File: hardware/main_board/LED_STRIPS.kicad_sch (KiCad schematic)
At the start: 9 parts, among them IC801 SN74AHCT125DBR, J801 Conn_01x03_Pin, J802 Conn_01x03_Pin

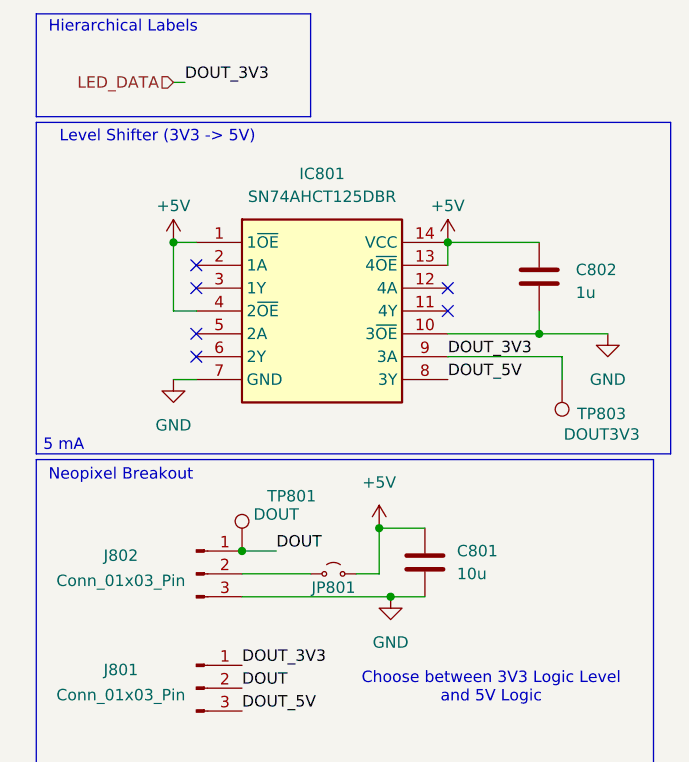
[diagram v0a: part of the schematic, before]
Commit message: changed level shifter. bunch of aesthetic changes. led resistors changed on main board. saving before nuke mouser.co.uk
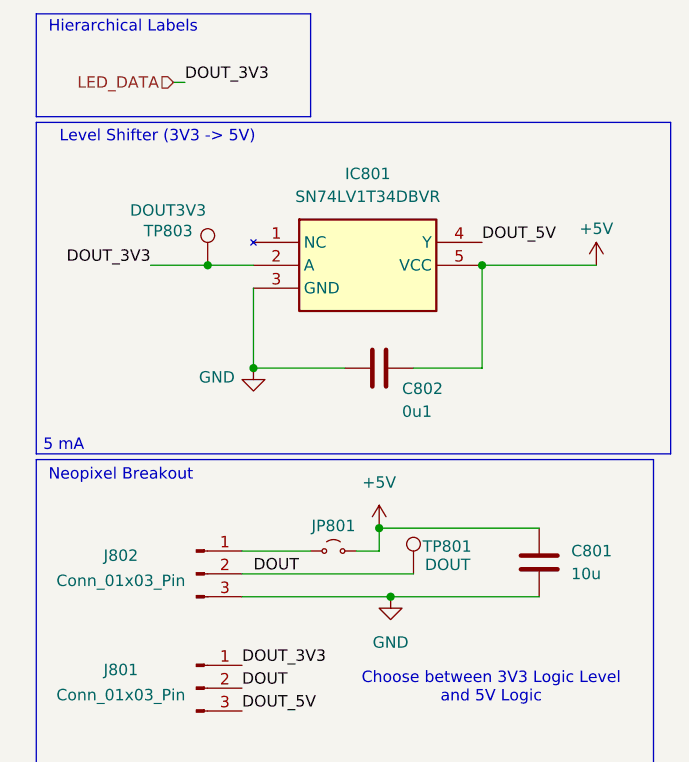
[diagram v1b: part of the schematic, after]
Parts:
- removed IC801: SN74AHCT125DBR, SamacSys_Parts:SOP65P780X200-14N, symbol SamacSys_Parts:SN74AHCT125DBR
- added IC801: SN74LV1T34DBVR, SamacSys_Parts:SOT95P280X145-5N, symbol SamacSys_Parts:SN74LV1T34DBVR
- C802: value 1u -> 0u1
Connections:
- net +5V: now also C802.2, IC801.5 (VCC); no longer C802.1
- net DOUT: now also J802.2 (Pin_2); no longer J802.1 (Pin_1)
- net DOUT_5V: now also IC801.4 (Y)
- net GND: now also C802.1, IC801.3 (GND); no longer C802.2
- net LED_DATA: now also IC801.2 (A)
- net at JP801.1 (A): now also J802.1 (Pin_1); no longer J802.2 (Pin_2)
- no-connect marks 6 -> 0
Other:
- moved on the sheet: C801, C802, JP801, TP801, TP803

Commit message: finished everything except bom information. drc verification
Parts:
- IC801: Mouser Price/Stock https://www.mouser.co.uk/ProductDetail/Texas-Instruments/SN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 -> https://www.mouser.com/ProductDetail/Texas-Instruments/SN74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
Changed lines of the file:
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@@
 			)
 		)
-		(property "Mouser Price/Stock" "https://www.mouser.co.uk/ProductDetail/Texas-Instruments/SN74LV1T34DBVR?qs=8sOby8ZxZLE4ekkxA3S6Wg%3D%3D"
+		(property "Mouser Price/Stock" "https://www.mouser.com/ProductDetail/Texas-Instruments/SN74LV1T34DBVR?qs=8sOby8ZxZLE4ekkxA3S6Wg%3D%3D"
 			(at 59.69 634.29 0)
 			(effects

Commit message: led info
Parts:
- C801: Mouser Price/Stock (none) -> https://www.mouser.com/ProductDetail/Samsung-Electro-Mechan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
- C802: Mouser Price/Stock (none) -> https://www.mouser.com/ProductDetail/Walsin/MG21B104K500CT?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
- U801: now left out of the parts list
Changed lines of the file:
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@@
+			)
+		)
+		(property "Mouser Price/Stock" "https://www.mouser.com/ProductDetail/Samsung-Electro-Mechanics/CL21A106KPFNNNE?qs=sGAEpiMZZMt7gvpyg0xT8jBAVP%252BdkPhuUJvUBe19zr8%3D"
+			(at 69.85 74.93 0)
+			(effects
+				(font
+					(size 1.27 1.27)
+				)
+				(hide yes)
 			)
 		)
@@
 		(unit 1)
 		(exclude_from_sim no)
-		(in_bom yes)
+		(in_bom no)
 		(on_board no)
 		(dnp no)
@@
 			(effects
 				(font
+					(size 1.27 1.27)
+				)
+				(hide yes)
+			)
+		)
+		(property "Mouser Price/Stock" "https://www.mouser.com/ProductDetail/Walsin/MG21B104K500CT?qs=sGAEpiMZZMt7gvpyg0xT8jBHDtGZvLzXjlSfFWC8Jgc2tQbZi0zprA%3D%3D"
+			(at 52.07 53.34 90)
+			(effects
+				(font

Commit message: up to date scheamtic
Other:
- note added: "I (Toby) fucked up and ordered the wrong level shifter lol just leave the footprint blank for now"
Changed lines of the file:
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@@
+		)
+	)
+	(text "I (Toby) fucked up and ordered the wrong level shifter lol\n\njust leave the footprint blank for now"
+		(exclude_from_sim no)
+		(at 162.814 50.8 0)
+		(effects
+			(font
+				(size 4 4)
+				(color 255 0 32 1)
+			)
 		)
 	)

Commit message: kys harddare
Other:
- note removed: "I (Toby) fucked up and ordered the wrong level shifter lol just leave the footprint blank for now"
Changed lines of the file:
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@@
-		)
-	)
-	(text "I (Toby) fucked up and ordered the wrong level shifter lol\n\njust leave the footprint blank for now"
-		(exclude_from_sim no)
-		(at 162.814 50.8 0)
-		(effects
-			(font
-				(size 4 4)
-				(color 255 0 32 1)
-			)
 		)
 	)
